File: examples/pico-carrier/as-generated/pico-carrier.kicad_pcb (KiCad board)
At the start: 2 copper layers, 80 x 56 mm, 9 parts, among them J1 5V IN, J3 GP0-GP15, J4 GP16-GP28, PWR, U1 Pico

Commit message: Never cut a corner off the pad it was there to reach
Once two routes meeting at a pad are merged into one run, the pad is an
interior corner of a polyline like any other, and the chamfer cut it -
moving the copper off the pad and leaving the net unconnected, which is
not something you can see in the shape. Both clean-up passes now hold
every pad and every track end still, from one list, for the same reason:
copper that something else is joined to is not theirs to move.

That is the last of the unconnected-net errors on the buck, the motor
and the opamp boards, and the 0 degree spur on the Pico's VSYS - which
was the failed half of a route to a pad the chamfer had already cut it
away from.
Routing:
- net /VSYS: track 33.6 -> 35.0 mm
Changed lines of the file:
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@@
 	(segment (start 148.0 66.5) (end 151.5 70.0) (width 0.25) (layer "F.Cu") (net 36))
 	(segment (start 151.5 70.0) (end 156.0 70.0) (width 0.25) (layer "F.Cu") (net 36))
-	(segment (start 156.0 70.0) (end 156.5 69.5) (width 0.25) (layer "F.Cu") (net 36))
-	(segment (start 156.5 69.5) (end 155.0 71.0) (width 0.25) (layer "F.Cu") (net 36))
+	(segment (start 156.0 70.0) (end 157.0 69.0) (width 0.25) (layer "F.Cu") (net 36))
+	(segment (start 157.0 69.0) (end 155.0 71.0) (width 0.25) (layer "F.Cu") (net 36))
 	(segment (start 155.0 71.0) (end 146.25 71.0) (width 0.25) (layer "F.Cu") (net 36))
 	(segment (start 146.25 71.0) (end 146.235 71.015) (width 0.25) (layer "F.Cu") (net 36))

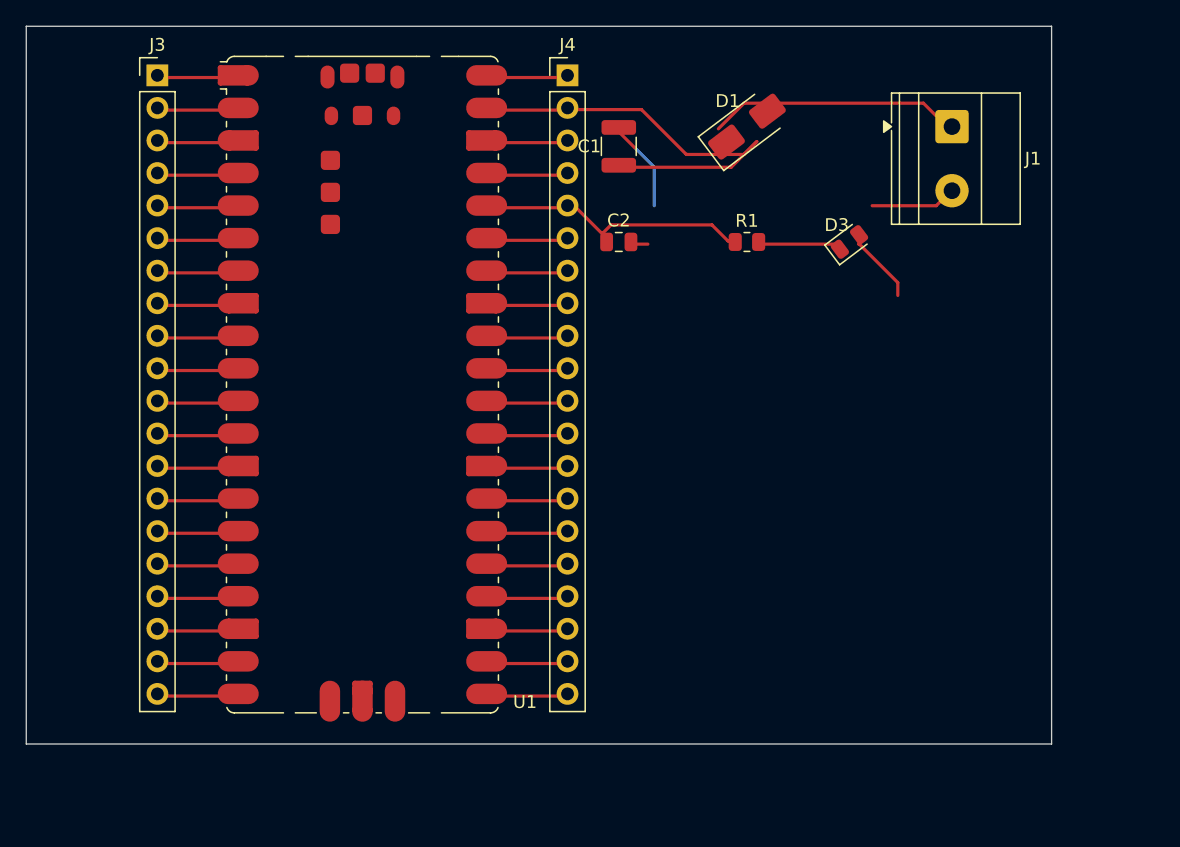
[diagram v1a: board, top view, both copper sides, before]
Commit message: Put the silkscreen where the board is not
Three legends were printed across pads. The board id was written at the
bottom centre whether or not the bottom centre was a module; the pin
names beside a connector went toward the middle of the board, which on a
carrier is the module they are labelling; and a footprint's designator
stayed where its library had drawn it, which on a part with pads down
both sides and along the bottom is the middle of a pad. Silk over a pad
is not a legend - the mask opens there, the ink comes off in
fabrication, and what is left is a pad that will not wet.

So all three ask first. The board id offers its usual spot and then the
next-best strips in turn. A pin name measures the *area* it would take
from other footprints on either side of the row and picks the smaller,
which chooses outboard on its own where there is an edge to face, and
matters because "half a legend over a module's pads" and "a tenth of a
millimetre into a chip capacitor's courtyard" are both one collision and
only one of them is a defect. A designator steps to the first spot in
its own footprint that no pad occupies.

Modules that draw no courtyard are measured by their pads instead:
taking a missing courtyard to mean the part occupies no board is how the
Pico's legend ended up across it.

The Pico carrier also grew: its two headers and the module run the
length of the board, and the plane could not get past their pin rows at
either end, so it was three islands with the return current going the
long way round. Six millimetres of board below the last pin is what a
plane needs to be one plane.
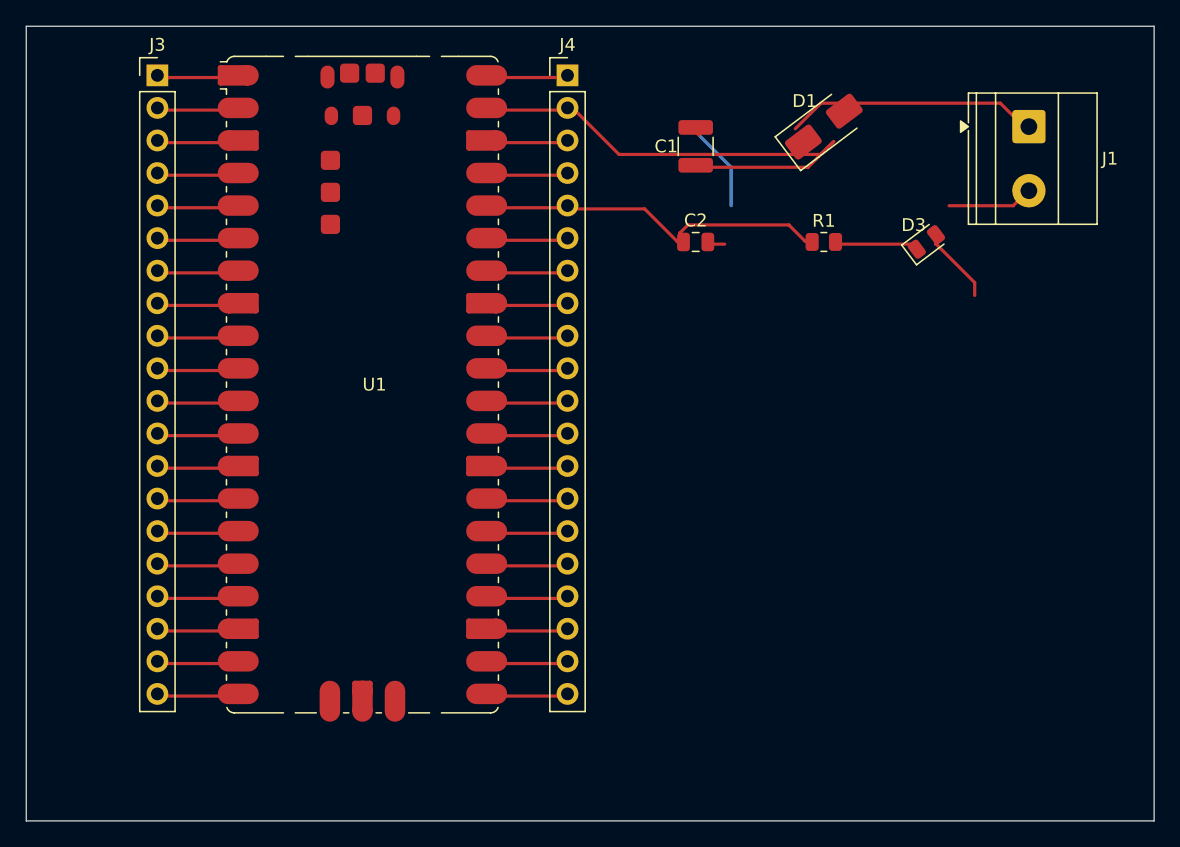
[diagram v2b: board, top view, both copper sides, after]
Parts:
- moved C1 6.00 mm to (152.2, 69.4)
- moved C2 6.00 mm to (152.2, 76.8)
- moved D1 6.00 mm to (162.2, 67.8)
- moved D3 6.00 mm to (170.2, 76.8)
- moved J1 6.00 mm to (178.2, 67.8)
- moved R1 6.00 mm to (162.2, 76.8)
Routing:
- net /VSYS: track 35.0 -> 41.0 mm
- net +3V3: track 22.8 -> 28.4 mm
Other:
- board size 80 x 56 mm -> 88 x 62 mm
